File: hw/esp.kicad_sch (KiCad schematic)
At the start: 12 parts, among them SW2 EN, SW3 BOOT, U5 ESP32-S3-WROOM

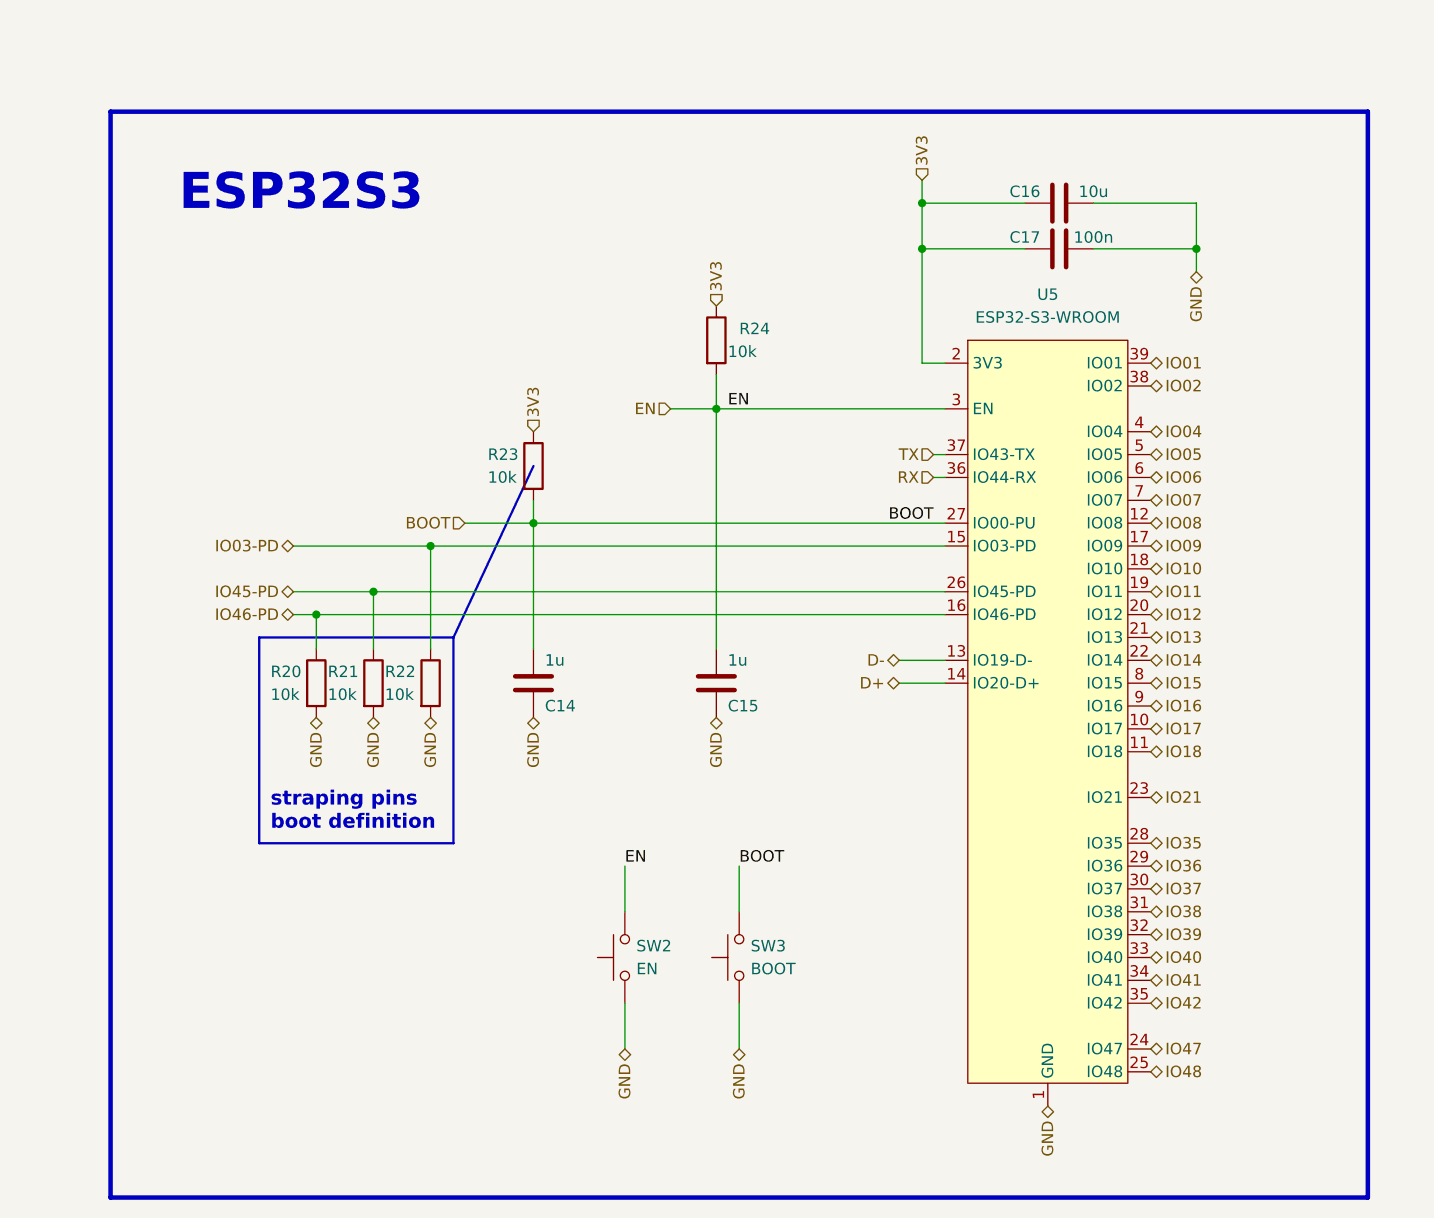
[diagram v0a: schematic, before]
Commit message: Graphic modifications of the scheme
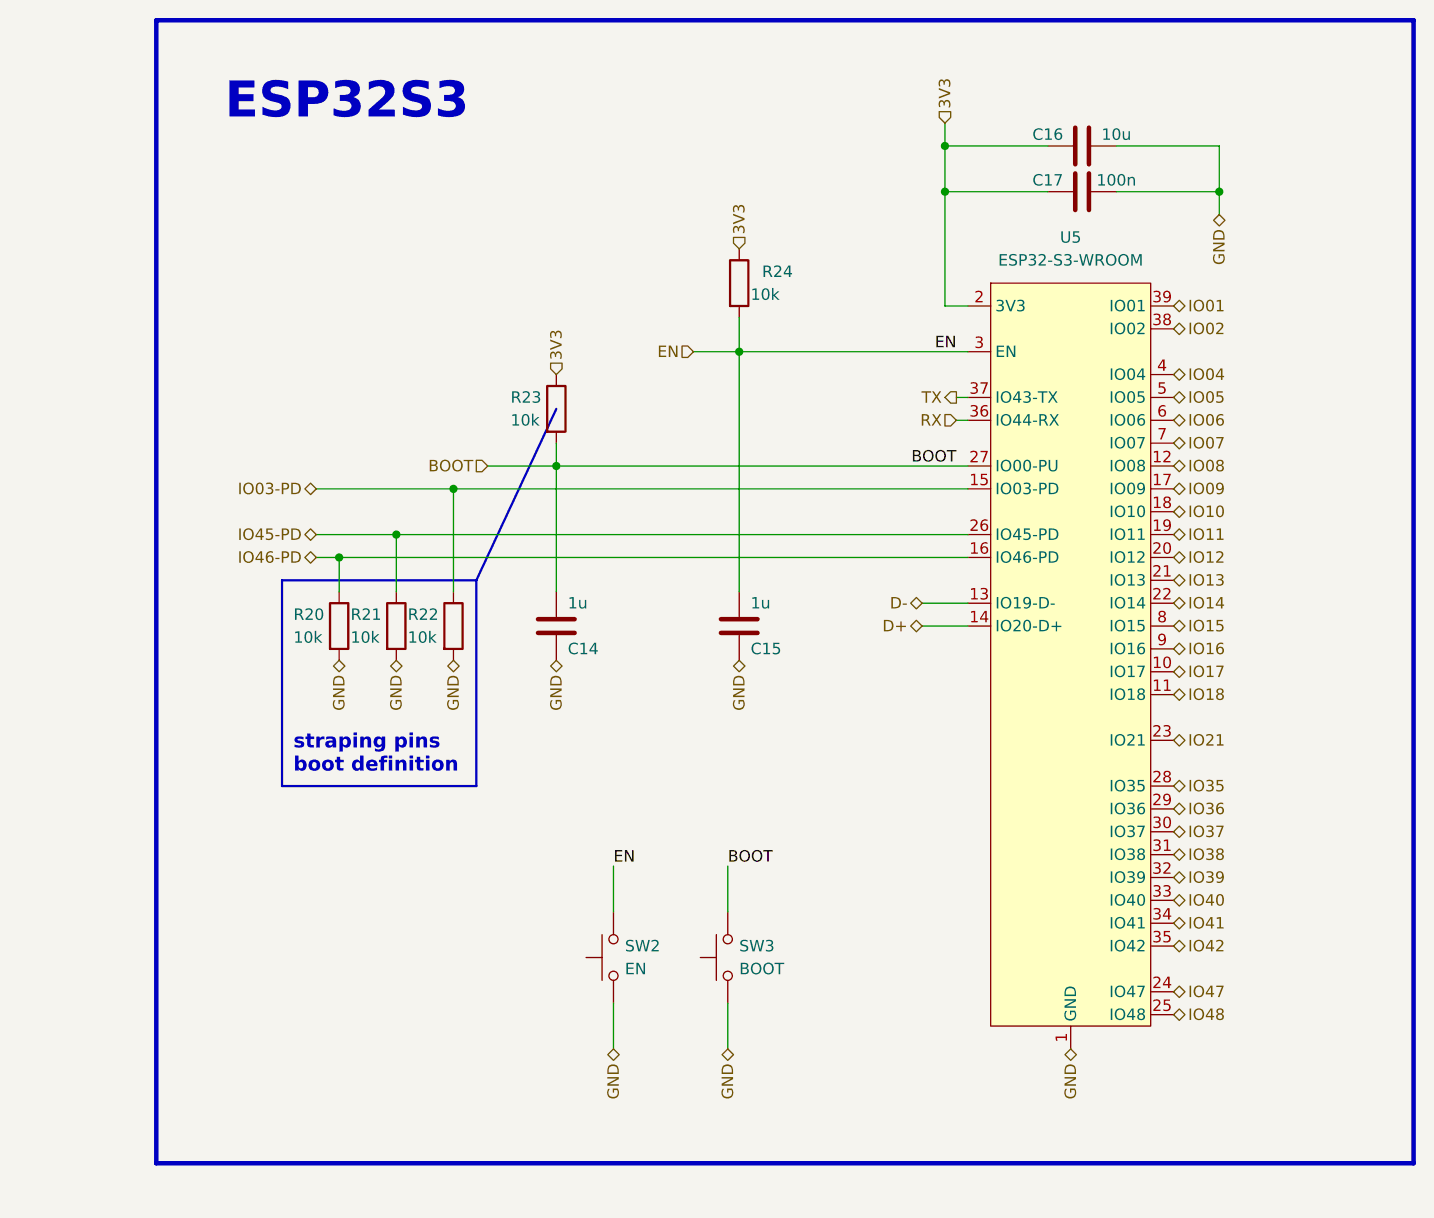
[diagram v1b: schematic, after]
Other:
- moved on the sheet: C14, C15, C16, C17, R20, R21, R22, R23, R24, SW2, SW3, U5

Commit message: add routing
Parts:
- SW2, SW3: footprint RLK-ElectorMechanicalComponents:TCF2QR -> RLK-ElectorMechanicalComponents:Tactile_switch
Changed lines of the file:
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@@
       (effects (font (size 1.27 1.27)) (justify right))
     )
-    (property "Footprint" "RLK-ElectorMechanicalComponents:TCF2QR" (at 134.62 129.54 0)
+    (property "Footprint" "RLK-ElectorMechanicalComponents:Tactile_switch" (at 134.62 129.54 0)
       (effects (font (size 1.27 1.27)) hide)
     )
@@
       (effects (font (size 1.27 1.27)) (justify right))
     )
-    (property "Footprint" "RLK-ElectorMechanicalComponents:TCF2QR" (at 121.92 129.54 0)
-      (effects (font (size 1.27 1.27)) hide)
-    )
+    (property "Footprint" "RLK-ElectorMechanicalComponents:Tactile_switch" (at 121.92 129.54 0)
+      (effects (font (size 1.27 1.27)) hide)
+    )

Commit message: Component inspection wip 0
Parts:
- added C20: 100n, Capacitor_SMD:C_0402_1005Metric, symbol Device:C
- added C31: 1u, Capacitor_SMD:C_0402_1005Metric, symbol Device:C
- added U10: SGM3001, Package_TO_SOT_SMD:SOT-363_SC-70-6, symbol RKL-SpecialThings:SGM3001
- C14, C15: Basic/Extended E -> B; LCSC C1518208 -> C52923; info 50V, X5R (potenciálně C52923 což je 25V, X5R ) -> 25V, X5R
- C17: LCSC C307331 -> C1525; info 50V, X7R -> 16V, X7R
- R20, R21, R22, R23, R24: JLCPCB_CORRECTION 0;0;0 -> (none)
- SW2, SW3: footprint RLK-ElectorMechanicalComponents:Tactile_switch -> Button_Switch_SMD:SW_Push_1P1T_NO_Vertical_Wuerth_434133025816; LCSC C240292 -> C127488
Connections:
- net 3V3: now also C20.1, U10.2 (V+)
- net EN: now also R22.1
- net GND: now also C20.2, C31.2, U10.3 (GND); no longer R22.2
- net IO03-PD: no longer names the net of U5.15 (IO03-PD)
- net IO03-PD: now also U10.6 (NO); no longer R22.1
- new net: C31.1, R22.2, U10.1 (IN)
- new net IO03: U10.5 (CON)
- no-connect marks 0 -> 1
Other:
- note removed: "ESP32S3"
- moved on the sheet: C14, C15, C16, C17, R20, R21, R23, R24, U5

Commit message: Inspection of parts complete
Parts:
- U5: LCSC C3013946 -> C2913202
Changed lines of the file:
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@@
       (effects (font (size 1.27 1.27)) hide)
     )
-    (property "LCSC" "C3013946" (at 179.07 43.18 0)
+    (property "LCSC" "C2913202" (at 179.07 43.18 0)
       (effects (font (size 1.27 1.27)) hide)
     )

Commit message: fuj fuj nepěkná věc
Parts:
- removed C20: 100n, Capacitor_SMD:C_0402_1005Metric, symbol Device:C
- removed C31: 1u, Capacitor_SMD:C_0402_1005Metric, symbol Device:C
- removed R22: 10k, Resistor_SMD:R_0402_1005Metric, symbol Device:R
- removed U10: SGM3001, Package_TO_SOT_SMD:SOT-363_SC-70-6, symbol RKL-SpecialThings:SGM3001
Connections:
- net IO03: now also U5.15 (IO03-PD)
- no-connect marks 1 -> 0

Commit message: Solved issue "Micro USB"
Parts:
- U5: JLCPCB_CORRECTION (none) -> 0;10;0
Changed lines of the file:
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@@
+      (effects (font (size 1.27 1.27)) hide)
+    )
+    (property "JLCPCB_CORRECTION" "0;10;0" (at 179.07 55.88 0)
       (effects (font (size 1.27 1.27)) hide)
     )

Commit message: JLCPCB_CORRECTION
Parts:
- U5: JLCPCB_CORRECTION 0;10;0 -> 0;11.2;0
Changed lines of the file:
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@@
       (effects (font (size 1.27 1.27)) hide)
     )
-    (property "JLCPCB_CORRECTION" "0;10;0" (at 179.07 55.88 0)
+    (property "JLCPCB_CORRECTION" "0;11.2;0" (at 179.07 55.88 0)
       (effects (font (size 1.27 1.27)) hide)
     )
